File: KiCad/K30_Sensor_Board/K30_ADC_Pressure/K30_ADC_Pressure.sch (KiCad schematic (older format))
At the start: 10 parts, among them J1 CONN_02X12, J2 CONN_01X03, J3 CONN_01X05, J4 CONN_01X03, U1 ADS1015_VSSOP, U2 LPS25HB_HLGA

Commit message: added decoupling capacitors for power input
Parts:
- added C4, C6: 0.1u, Capacitors_SMD:C_0603_HandSoldering, symbol C
- added C5, C7: 10u, Capacitors_SMD:CP_Elec_5x4.5, symbol CP1
- added D1, D2: LED, LEDs:LED_0603_HandSoldering, symbol LED
- added R2, R3: 2.2k, Resistors_SMD:R_0603_HandSoldering, symbol R
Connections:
- net 3V3: now also C6.1, C7.1, D2.2 (A)
- net 5V: now also C4.1, C5.1, D1.2 (A)
- net GND: now also C4.2, C5.2, C6.2, C7.2, R2.1, R3.1
- new net: D1.1 (K), R2.2
- new net: D2.1 (K), R3.2
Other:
- moved on the sheet: C2, J3

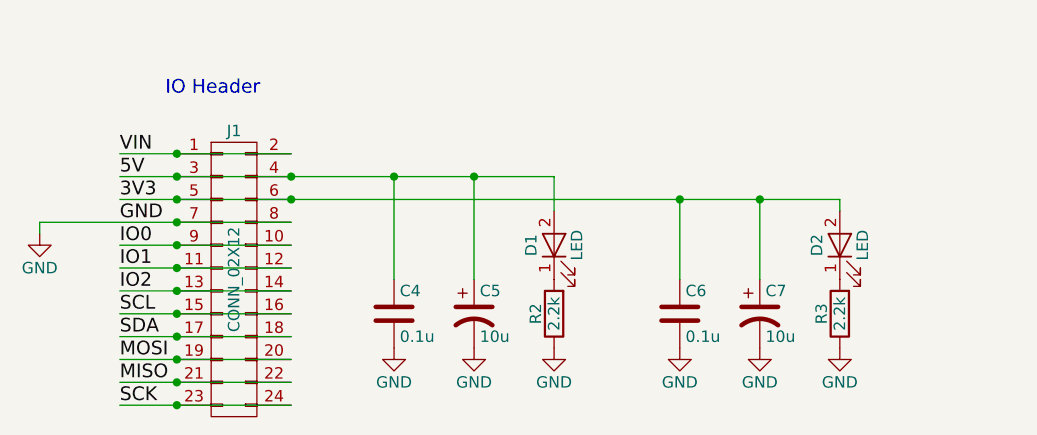
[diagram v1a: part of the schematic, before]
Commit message: remove leds, new gerber files
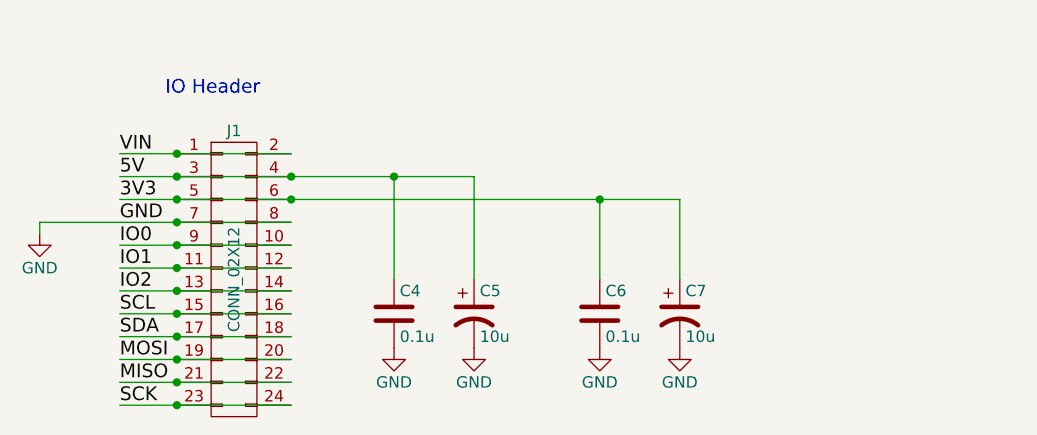
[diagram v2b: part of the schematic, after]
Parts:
- removed D1, D2: LED, LEDs:LED_0603_HandSoldering, symbol LED
- removed R2, R3: 2.2k, Resistors_SMD:R_0603_HandSoldering, symbol R
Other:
- moved on the sheet: C6, C7
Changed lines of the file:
@@
-$EndComp
-$Comp
-L LED D1
-U 1 1 5963F669
-P 3500 6050
-F 0 "D1" H 3500 6150 50  0000 C CNN
-F 1 "LED" H 3500 5950 50  0000 C CNN
-F 2 "LEDs:LED_0603_HandSoldering" H 3500 6050 50  0001 C CNN
-F 3 "" H 3500 6050 50  0001 C CNN
-	1    3500 6050
-	0    -1   -1   0
 $EndComp
 $Comp
@@
 $EndComp
 $Comp
-L R R2
-U 1 1 59640D98
-P 3500 6350
-F 0 "R2" V 3580 6350 50  0000 C CNN
-F 1 "2.2k" V 3500 6350 50  0000 C CNN
-F 2 "Resistors_SMD:R_0603_HandSoldering" V 3430 6350 50  0001 C CNN
-F 3 "" H 3500 6350 50  0001 C CNN
-	1    3500 6350
-	-1   0    0    1
-$EndComp
-$Comp
-L GND #PWR09
-U 1 1 596411FE
-P 3500 6500
-F 0 "#PWR09" H 3500 6250 50  0001 C CNN
-F 1 "GND" H 3500 6350 50  0000 C CNN
-F 2 "" H 3500 6500 50  0001 C CNN
-F 3 "" H 3500 6500 50  0001 C CNN
-	1    3500 6500
-	1    0    0    -1
-$EndComp
-$Comp
 L C C6
 U 1 1 596426B0
+P 3700 6350
+F 0 "C6" H 3725 6450 50  0000 L CNN
+F 1 "0.1u" H 3725 6250 50  0000 L CNN
+F 2 "Capacitors_SMD:C_0603_HandSoldering" H 3738 6200 50  0001 C CNN
+F 3 "" H 3700 6350 50  0001 C CNN
+	1    3700 6350
+	1    0    0    -1
+$EndComp
+$Comp
+L CP1 C7
+U 1 1 59642711
 P 4050 6350
-F 0 "C6" H 4075 6450 50  0000 L CNN
-F 1 "0.1u" H 4075 6250 50  0000 L CNN
-F 2 "Capacitors_SMD:C_0603_HandSoldering" H 4088 6200 50  0001 C CNN
+F 0 "C7" H 4075 6450 50  0000 L CNN
+F 1 "10u" H 4075 6250 50  0000 L CNN
+F 2 "Capacitors_SMD:CP_Elec_5x4.5" H 4050 6350 50  0001 C CNN
 F 3 "" H 4050 6350 50  0001 C CNN
 	1    4050 6350
@@
 $EndComp
 $Comp
-L CP1 C7
-U 1 1 59642711
-P 4400 6350
-F 0 "C7" H 4425 6450 50  0000 L CNN
-F 1 "10u" H 4425 6250 50  0000 L CNN
-F 2 "Capacitors_SMD:CP_Elec_5x4.5" H 4400 6350 50  0001 C CNN
-F 3 "" H 4400 6350 50  0001 C CNN
-	1    4400 6350
-	1    0    0    -1
-$EndComp
-$Comp
-L R R3
-U 1 1 596427B5
-P 4750 6350
-F 0 "R3" V 4830 6350 50  0000 C CNN
-F 1 "2.2k" V 4750 6350 50  0000 C CNN
-F 2 "Resistors_SMD:R_0603_HandSoldering" V 4680 6350 50  0001 C CNN
-F 3 "" H 4750 6350 50  0001 C CNN
-	1    4750 6350
-	-1   0    0    1
-$EndComp
-$Comp
-L LED D2
-U 1 1 59642828
-P 4750 6050
-F 0 "D2" H 4750 6150 50  0000 C CNN
-F 1 "LED" H 4750 5950 50  0000 C CNN
-F 2 "LEDs:LED_0603_HandSoldering" H 4750 6050 50  0001 C CNN
-F 3 "" H 4750 6050 50  0001 C CNN
-	1    4750 6050
-	0    -1   -1   0
+L GND #PWR09
+U 1 1 5964288A
+P 3700 6500
+F 0 "#PWR09" H 3700 6250 50  0001 C CNN
+F 1 "GND" H 3700 6350 50  0000 C CNN
+F 2 "" H 3700 6500 50  0001 C CNN
+F 3 "" H 3700 6500 50  0001 C CNN
+	1    3700 6500
+	1    0    0    -1
 $EndComp
 $Comp
 L GND #PWR010
-U 1 1 5964288A
+U 1 1 596428CB
 P 4050 6500
 F 0 "#PWR010" H 4050 6250 50  0001 C CNN
@@
 	1    0    0    -1
 $EndComp
-$Comp
-L GND #PWR011
-U 1 1 596428CB
-P 4400 6500
-F 0 "#PWR011" H 4400 6250 50  0001 C CNN
-F 1 "GND" H 4400 6350 50  0000 C CNN
-F 2 "" H 4400 6500 50  0001 C CNN
-F 3 "" H 4400 6500 50  0001 C CNN
-	1    4400 6500
-	1    0    0    -1
-$EndComp
-$Comp
-L GND #PWR012
-U 1 1 5964290C
-P 4750 6500
-F 0 "#PWR012" H 4750 6250 50  0001 C CNN
-F 1 "GND" H 4750 6350 50  0000 C CNN
-F 2 "" H 4750 6500 50  0001 C CNN
-F 3 "" H 4750 6500 50  0001 C CNN
-	1    4750 6500
-	1    0    0    -1
-$EndComp
 Wire Wire Line
 	3100 2400 3600 2400
@@
 Connection ~ 2950 2700
 Connection ~ 3400 2900
-Wire Wire Line
-	1600 5750 3500 5750
 Connection ~ 2350 5750
 Wire Wire Line
@@
 Connection ~ 2350 5850
 Wire Wire Line
-	3500 5750 3500 5900
-Connection ~ 3150 5750
-Wire Wire Line
 	2800 5750 2800 6200
 Connection ~ 2800 5750
 Wire Wire Line
-	1600 5850 4750 5850
-Wire Wire Line
-	4750 5850 4750 5900
+	3700 6200 3700 5850
+Connection ~ 3700 5850
 Wire Wire Line
 	4050 6200 4050 5850
-Connection ~ 4050 5850
-Wire Wire Line
-	4400 6200 4400 5850
-Connection ~ 4400 5850
-$Comp
-L GND #PWR013
+$Comp
+L GND #PWR011
 U 1 1 59643860
 P 8100 5700
-F 0 "#PWR013" H 8100 5450 50  0001 C CNN
+F 0 "#PWR011" H 8100 5450 50  0001 C CNN
 F 1 "GND" H 8100 5550 50  0000 C CNN
 F 2 "" H 8100 5700 50  0001 C CNN
@@
 	8100 5600 8100 5700
 $Comp
-L GND #PWR014
+L GND #PWR012
 U 1 1 596439D5
 P 7900 5700
-F 0 "#PWR014" H 7900 5450 50  0001 C CNN
+F 0 "#PWR012" H 7900 5450 50  0001 C CNN
 F 1 "GND" H 7900 5550 50  0000 C CNN
 F 2 "" H 7900 5700 50  0001 C CNN
@@
 Wire Wire Line
 	7900 5150 7900 5700
+Wire Wire Line
+	1600 5750 3150 5750
+Wire Wire Line
+	4050 5850 1600 5850
 $EndSCHEMATC
